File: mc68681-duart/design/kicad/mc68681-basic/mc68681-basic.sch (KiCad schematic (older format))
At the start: 33 parts, among them IC1 68681, IC2 74HCT245, IC3 74HCT245, IC4 74HCT245, IC5 74125, IC6 IC6_DECO.PLD, IC7 IC7_UART_.PLD, J1 Conn_02x32_Odd_Even, J2 EXTBUS, J3 UART_A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

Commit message: Initial work on schematic, board ripped up
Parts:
- removed IC1: 68681, Package_DIP:DIP-40_W15.24mm_Socket_LongPads, symbol Interface:68681
- removed JP1, JP2, JP3, JP4: Jumper, Connector_PinHeader_2.54mm:PinHeader_1x02_P2.54mm_Vertical, symbol Device:Jumper
- added IC1: XR68C681CJTR-F, Package_LCC:PLCC-44_THT-Socket, symbol XR68C681:XR68C681CJTR-F
- added JP1-5: Conn_02x05_Odd_Even, Connector_PinHeader_2.54mm:PinHeader_2x05_P2.54mm_Vertical, symbol Connector_Generic:Conn_02x05_Odd_Even
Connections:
- net labels added: IACK, UVPA
- wire segments 142 -> 150
- no-connect marks 43 -> 39
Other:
- moved on the sheet: C3, C5, J3, J4, Q1, R1, R2

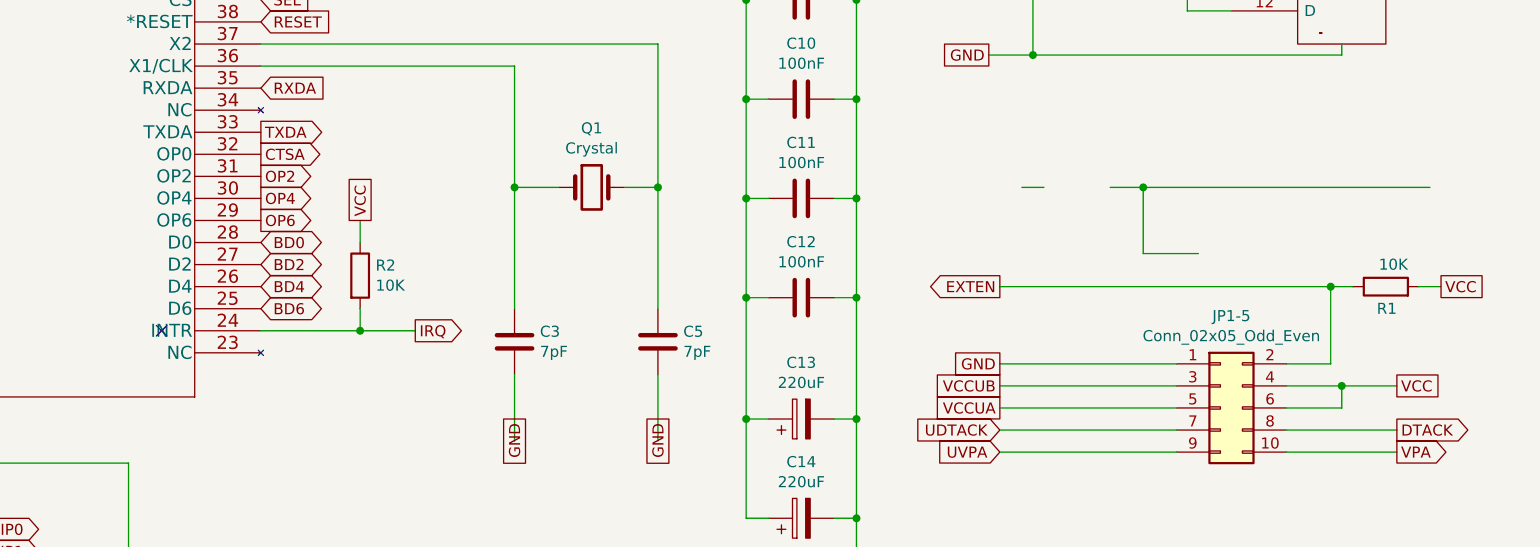
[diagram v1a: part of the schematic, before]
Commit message: First cut redo 68681 layout, add lib and pretty
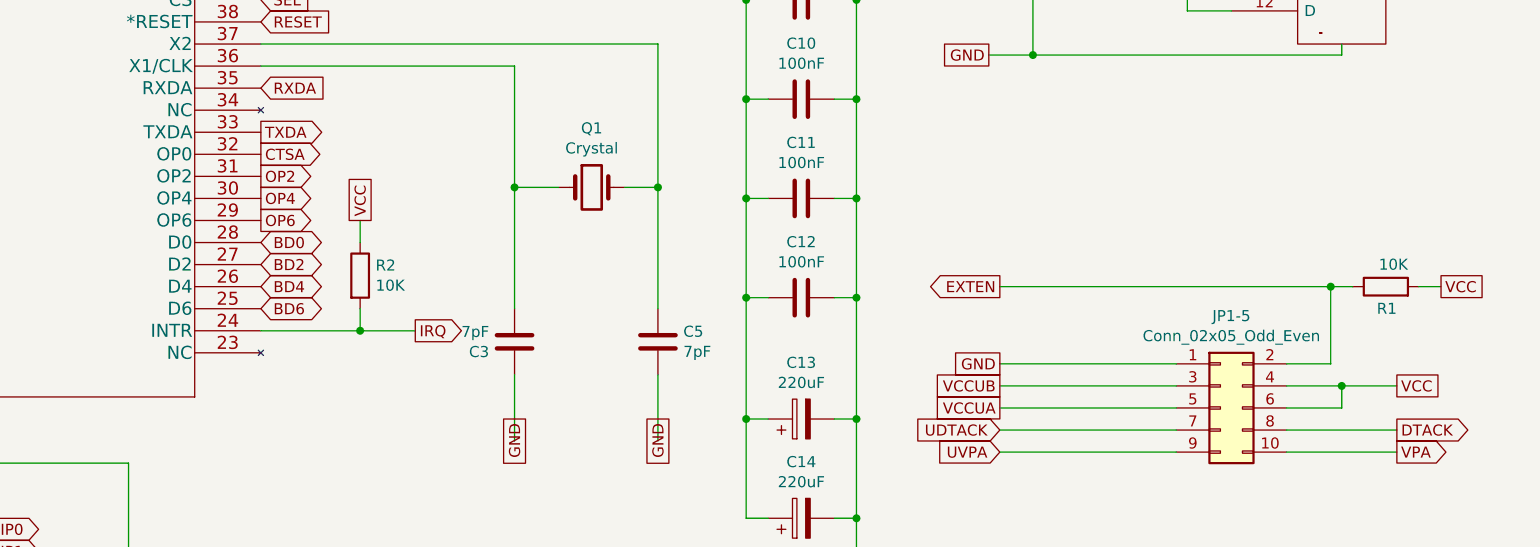
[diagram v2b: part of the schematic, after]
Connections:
- wire segments 150 -> 145
- no-connect marks 39 -> 38
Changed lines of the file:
@@
 F 3 "~" H 6550 5150 50  0001 C CNN
 	1    6550 5150
-	1    0    0    -1
+	-1   0    0    1
 $EndComp
 $Comp
@@
 Text GLabel 10750 4900 2    50   UnSpc ~ 0
 VCC
-Wire Wire Line
-	9400 4450 10700 4450
 Connection ~ 7200 4450
 Text GLabel 3400 4300 0    50   Output ~ 0
@@
 NoConn ~ 1050 2000
 NoConn ~ 1550 2400
-NoConn ~ 4950 5100
 Text GLabel 5400 3100 2    50   UnSpc ~ 0
 VCC
@@
 $EndComp
 Wire Wire Line
-	9250 4450 9400 4450
-Connection ~ 9400 4450
-Wire Wire Line
-	8850 4450 8950 4450
-Wire Wire Line
 	9800 2700 9600 2700
 Wire Wire Line
@@
 Text GLabel 8750 5650 0    50   Input ~ 0
 UVPA
-Wire Wire Line
-	9400 4450 9400 4750
 Text GLabel 5400 3400 2    50   Input ~ 0
 IACK
@@
 $EndComp
 Wire Wire Line
-	9400 4750 9650 4750
-Wire Wire Line
 	10550 5350 10300 5350

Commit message: Fix 7pF footprint & prep for prototype fab
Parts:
- C3, C5: footprint rosco_m68k:C2.5-3 -> Capacitor_THT:C_Rect_L7.0mm_W2.0mm_P5.00mm
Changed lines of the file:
@@
 F 0 "C3" H 6665 5196 50  0000 L CNN
 F 1 "7pF" H 6665 5105 50  0000 L CNN
-F 2 "rosco_m68k:C2.5-3" H 6588 5000 50  0001 C CNN
+F 2 "Capacitor_THT:C_Rect_L7.0mm_W2.0mm_P5.00mm" H 6588 5000 50  0001 C CNN
 F 3 "~" H 6550 5150 50  0001 C CNN
 	1    6550 5150
@@
 F 0 "C5" H 7315 5196 50  0000 L CNN
 F 1 "7pF" H 7315 5105 50  0000 L CNN
-F 2 "rosco_m68k:C2.5-3" H 7238 5000 50  0001 C CNN
+F 2 "Capacitor_THT:C_Rect_L7.0mm_W2.0mm_P5.00mm" H 7238 5000 50  0001 C CNN
 F 3 "~" H 7200 5150 50  0001 C CNN
 	1    7200 5150
